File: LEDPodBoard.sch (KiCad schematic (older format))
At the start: 10 parts

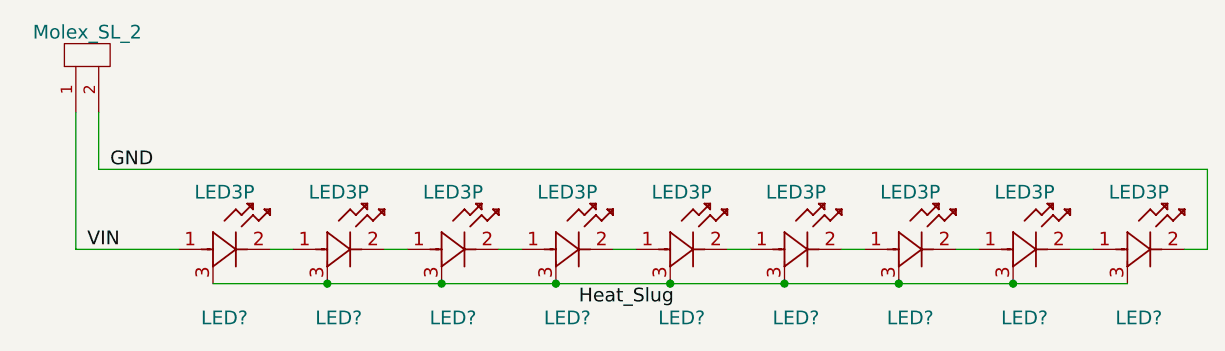
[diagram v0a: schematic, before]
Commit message: Placed LEDs
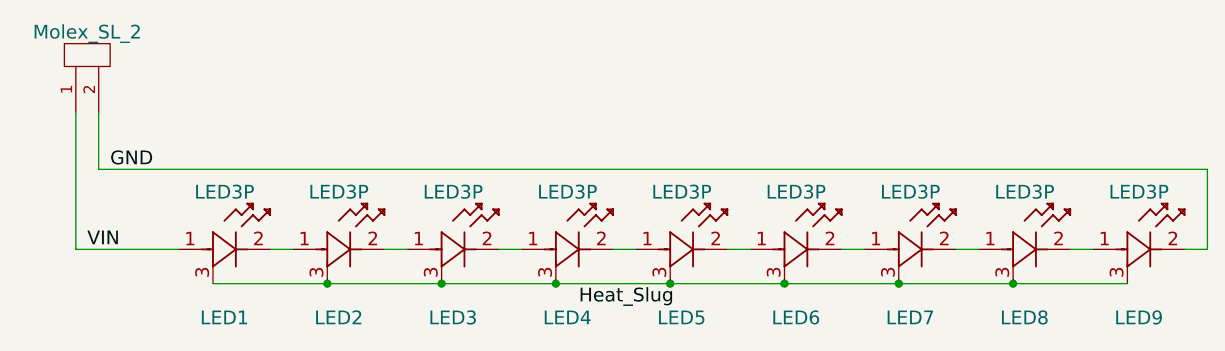
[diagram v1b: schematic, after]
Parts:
- Conn1: renamed from Conn?; footprint (none) -> MRDT_Connectors:MOLEX_SL_2_Horizontal
- LED1, LED2, LED3, LED4, LED5, LED6, LED7, LED8, LED9: renamed from LED?; footprint LED_CREE_XLAMP_XPG -> MRDT_Actives:LED_CREE_XLAMP_XPG
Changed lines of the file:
@@
 LIBS:MRDT_Silkscreens
 LIBS:MRDT_Switches
+LIBS:LEDPodBoard-cache
 EELAYER 25 0
 EELAYER END
@@
 $EndDescr
 $Comp
-L LED3P LED?
+L LED3P LED1
 U 1 1 5ADC1597
 P 1950 2050
-F 0 "LED?" H 2150 1750 60  0000 C CNN
+F 0 "LED1" H 2150 1750 60  0000 C CNN
 F 1 "LED3P" H 2150 2300 60  0000 C CNN
-F 2 "LED_CREE_XLAMP_XPG" H 2150 2400 60  0001 C CNN
+F 2 "MRDT_Actives:LED_CREE_XLAMP_XPG" H 2150 2400 60  0001 C CNN
 F 3 "" H 1950 2050 60  0000 C CNN
 	1    1950 2050
@@
 $EndComp
 $Comp
-L LED3P LED?
+L LED3P LED2
 U 1 1 5ADC1629
 P 2450 2050
-F 0 "LED?" H 2650 1750 60  0000 C CNN
+F 0 "LED2" H 2650 1750 60  0000 C CNN
 F 1 "LED3P" H 2650 2300 60  0000 C CNN
-F 2 "LED_CREE_XLAMP_XPG" H 2650 2400 60  0001 C CNN
+F 2 "MRDT_Actives:LED_CREE_XLAMP_XPG" H 2650 2400 60  0001 C CNN
 F 3 "" H 2450 2050 60  0000 C CNN
 	1    2450 2050
@@
 $EndComp
 $Comp
-L LED3P LED?
+L LED3P LED3
 U 1 1 5ADC169D
 P 2950 2050
-F 0 "LED?" H 3150 1750 60  0000 C CNN
+F 0 "LED3" H 3150 1750 60  0000 C CNN
 F 1 "LED3P" H 3150 2300 60  0000 C CNN
-F 2 "LED_CREE_XLAMP_XPG" H 3150 2400 60  0001 C CNN
+F 2 "MRDT_Actives:LED_CREE_XLAMP_XPG" H 3150 2400 60  0001 C CNN
 F 3 "" H 2950 2050 60  0000 C CNN
 	1    2950 2050
@@
 $EndComp
 $Comp
-L LED3P LED?
+L LED3P LED4
 U 1 1 5ADC16D0
 P 3450 2050
-F 0 "LED?" H 3650 1750 60  0000 C CNN
+F 0 "LED4" H 3650 1750 60  0000 C CNN
 F 1 "LED3P" H 3650 2300 60  0000 C CNN
-F 2 "LED_CREE_XLAMP_XPG" H 3650 2400 60  0001 C CNN
+F 2 "MRDT_Actives:LED_CREE_XLAMP_XPG" H 3650 2400 60  0001 C CNN
 F 3 "" H 3450 2050 60  0000 C CNN
 	1    3450 2050
@@
 $EndComp
 $Comp
-L LED3P LED?
+L LED3P LED5
 U 1 1 5ADC1702
 P 3950 2050
-F 0 "LED?" H 4150 1750 60  0000 C CNN
+F 0 "LED5" H 4150 1750 60  0000 C CNN
 F 1 "LED3P" H 4150 2300 60  0000 C CNN
-F 2 "LED_CREE_XLAMP_XPG" H 4150 2400 60  0001 C CNN
+F 2 "MRDT_Actives:LED_CREE_XLAMP_XPG" H 4150 2400 60  0001 C CNN
 F 3 "" H 3950 2050 60  0000 C CNN
 	1    3950 2050
@@
 $EndComp
 $Comp
-L LED3P LED?
+L LED3P LED6
 U 1 1 5ADC173F
 P 4450 2050
-F 0 "LED?" H 4650 1750 60  0000 C CNN
+F 0 "LED6" H 4650 1750 60  0000 C CNN
 F 1 "LED3P" H 4650 2300 60  0000 C CNN
-F 2 "LED_CREE_XLAMP_XPG" H 4650 2400 60  0001 C CNN
+F 2 "MRDT_Actives:LED_CREE_XLAMP_XPG" H 4650 2400 60  0001 C CNN
 F 3 "" H 4450 2050 60  0000 C CNN
 	1    4450 2050
@@
 $EndComp
 $Comp
-L LED3P LED?
+L LED3P LED7
 U 1 1 5ADC1775
 P 4950 2050
-F 0 "LED?" H 5150 1750 60  0000 C CNN
+F 0 "LED7" H 5150 1750 60  0000 C CNN
 F 1 "LED3P" H 5150 2300 60  0000 C CNN
-F 2 "LED_CREE_XLAMP_XPG" H 5150 2400 60  0001 C CNN
+F 2 "MRDT_Actives:LED_CREE_XLAMP_XPG" H 5150 2400 60  0001 C CNN
 F 3 "" H 4950 2050 60  0000 C CNN
 	1    4950 2050
@@
 $EndComp
 $Comp
-L LED3P LED?
+L LED3P LED8
 U 1 1 5ADC17B0
 P 5450 2050
-F 0 "LED?" H 5650 1750 60  0000 C CNN
+F 0 "LED8" H 5650 1750 60  0000 C CNN
 F 1 "LED3P" H 5650 2300 60  0000 C CNN
-F 2 "LED_CREE_XLAMP_XPG" H 5650 2400 60  0001 C CNN
+F 2 "MRDT_Actives:LED_CREE_XLAMP_XPG" H 5650 2400 60  0001 C CNN
 F 3 "" H 5450 2050 60  0000 C CNN
 	1    5450 2050
@@
 $EndComp
 $Comp
-L LED3P LED?
+L LED3P LED9
 U 1 1 5ADC17EC
 P 5950 2050
-F 0 "LED?" H 6150 1750 60  0000 C CNN
+F 0 "LED9" H 6150 1750 60  0000 C CNN
 F 1 "LED3P" H 6150 2300 60  0000 C CNN
-F 2 "LED_CREE_XLAMP_XPG" H 6150 2400 60  0001 C CNN
+F 2 "MRDT_Actives:LED_CREE_XLAMP_XPG" H 6150 2400 60  0001 C CNN
 F 3 "" H 5950 2050 60  0000 C CNN
 	1    5950 2050
@@
 	1500 2050 1950 2050
 $Comp
-L Molex_SL_2 Conn?
+L Molex_SL_2 Conn1
 U 1 1 5ADC1FE2
 P 1650 1250
-F 0 "Conn?" H 1700 1200 60  0001 C CNN
+F 0 "Conn1" H 1700 1200 60  0001 C CNN
 F 1 "Molex_SL_2" V 1800 1350 60  0000 C CNN
-F 2 "" H 1650 1150 60  0001 C CNN
+F 2 "MRDT_Connectors:MOLEX_SL_2_Horizontal" H 1650 1150 60  0001 C CNN
 F 3 "" H 1650 1150 60  0001 C CNN
 	1    1650 1250

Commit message: Routed and added silkscreen
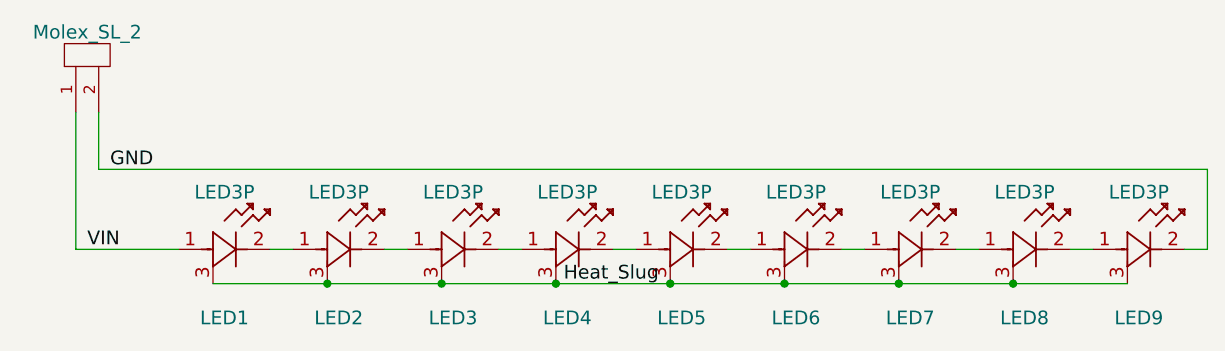
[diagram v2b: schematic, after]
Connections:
- net Heat_Slug: now also LED1.3 (Heat_Dissipation), LED2.3 (Heat_Dissipation), LED3.3 (Heat_Dissipation), LED4.3 (Heat_Dissipation), LED5.3 (Heat_Dissipation), LED6.3 (Heat_Dissipation), LED7.3 (Heat_Dissipation), LED8.3 (Heat_Dissipation), LED9.3 (Heat_Dissipation)
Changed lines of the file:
@@
 	0    -1   -1   0
 $EndComp
-Text Label 3700 2300 0    60   ~ 0
+Text Label 4050 2200 2    60   ~ 0
 Heat_Slug
 Wire Wire Line
